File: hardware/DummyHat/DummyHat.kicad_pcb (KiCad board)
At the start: 2 copper layers, 1 part, among them U1 7404

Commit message: Finish First Dummy Hat Design
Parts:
- added D1: D, Diode_THT:D_DO-34_SOD68_P7.62mm_Horizontal, F.Cu at (58.4, 91.9)
- added D2: D, Diode_THT:D_DO-34_SOD68_P7.62mm_Horizontal, F.Cu at (81.3, 91.9)
- added D3: D, Diode_THT:D_DO-34_SOD68_P7.62mm_Horizontal, F.Cu at (81.3, 101.6)
- added D4: D, Diode_THT:D_DO-34_SOD68_P7.62mm_Horizontal, F.Cu at (58.4, 101.6)
- added D5: D, Diode_THT:D_DO-34_SOD68_P7.62mm_Horizontal, F.Cu at (66.0, 108.2)
- added D6: LED, LED_THT:LED_D5.0mm, F.Cu at (59.2, 63.5)
- added D7: LED, LED_THT:LED_D5.0mm, F.Cu at (66.3, 63.5)
- added D8: LED, LED_THT:LED_D5.0mm, F.Cu at (73.4, 63.5)
- added D9: LED, LED_THT:LED_D5.0mm, F.Cu at (80.5, 63.5)
- added J1: Conn_01x08_Socket, Connector_PinSocket_2.54mm:PinSocket_1x08_P2.54mm_Vertical, F.Cu at (61.0, 112.0)
- added J2: Conn_01x08_Socket, Connector_PinSocket_2.54mm:PinSocket_1x08_P2.54mm_Vertical, F.Cu at (61.0, 56.6)
- added J3: Conn_01x08_Socket, Connector_PinSocket_2.54mm:PinSocket_1x08_P2.54mm_Vertical, F.Cu at (61.0, 53.1)
- added R1: R, Resistor_THT:R_Axial_DIN0207_L6.3mm_D2.5mm_P10.16mm_Horizontal, F.Cu at (59.2, 66.8)
- added R2: R, Resistor_THT:R_Axial_DIN0207_L6.3mm_D2.5mm_P10.16mm_Horizontal, F.Cu at (66.3, 66.8)
- added R3: R, Resistor_THT:R_Axial_DIN0207_L6.3mm_D2.5mm_P10.16mm_Horizontal, F.Cu at (73.4, 66.8)
- added R4: R, Resistor_THT:R_Axial_DIN0207_L6.3mm_D2.5mm_P10.16mm_Horizontal, F.Cu at (80.5, 66.8)
- U1: value 7404 -> 74HC04
- moved U1 100.8 mm to (62.2, 104.6), turned to -90 degrees
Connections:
- U1 pad 1: unconnected-(U1-Pad1) -> I0
- U1 pad 11: unconnected-(U1-Pad11) -> GND
- U1 pad 12: unconnected-(U1-Pad12) -> RESP
- U1 pad 13: unconnected-(U1-Pad13) -> Net-(D1-K)
- U1 pad 2: unconnected-(U1-Pad2) -> Net-(D1-A)
- U1 pad 3: unconnected-(U1-Pad3) -> GND
- U1 pad 5: unconnected-(U1-Pad5) -> GND
- U1 pad 9: unconnected-(U1-Pad9) -> GND
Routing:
- net GND: track 0.00 -> 81.6 mm
- net Net-(D1-K): track 0.00 -> 50.6 mm
- net I0: track 0.00 -> 23.2 mm
- net I1: track 0.00 -> 21.8 mm
- net Net-(D1-A): track 0.00 -> 17.6 mm
- net I2: track 0.00 -> 13.9 mm
- net I3: track 0.00 -> 13.9 mm
- net D3: track 0.00 -> 13.7 mm
- net D2: track 0.00 -> 9.16 mm
- net RESP: track 0.00 -> 8.94 mm
- net +5V: track 0.00 -> 7.89 mm
- net D1: track 0.00 -> 5.50 mm
- net D0: track 0.00 -> 5.08 mm
- net I4: track 0.00 -> 3.81 mm
- net Net-(D9-K): track 0.00 -> 3.30 mm
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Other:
- board outline added: 38.1 x 63.5 mm

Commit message: Finish dev board. Limitations still apply.
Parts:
- added D10: LED, LED_THT:LED_D5.0mm, F.Cu at (59.4, 119.1)
- added D11: LED, LED_THT:LED_D5.0mm, F.Cu at (69.1, 119.1)
- added D12: LED, LED_THT:LED_D5.0mm, F.Cu at (78.7, 119.1)
- added D13: LED, LED_THT:LED_D5.0mm, F.Cu at (59.4, 130.3)
- added D14: LED, LED_THT:LED_D5.0mm, F.Cu at (69.1, 130.3)
- added D15: LED, LED_THT:LED_D5.0mm, F.Cu at (78.7, 130.3)
- added R10: R, Resistor_THT:R_Axial_DIN0207_L6.3mm_D2.5mm_P10.16mm_Horizontal, F.Cu at (64.3, 129.5)
- added R11: R, Resistor_THT:R_Axial_DIN0207_L6.3mm_D2.5mm_P10.16mm_Horizontal, F.Cu at (73.9, 129.5)
- added R12: R, Resistor_THT:R_Axial_DIN0207_L6.3mm_D2.5mm_P10.16mm_Horizontal, F.Cu at (83.6, 129.5)
- added R13: R, Resistor_THT:R_Axial_DIN0207_L6.3mm_D2.5mm_P10.16mm_Horizontal, F.Cu at (54.9, 133.9)
- added R14: R, Resistor_THT:R_Axial_DIN0207_L6.3mm_D2.5mm_P10.16mm_Horizontal, F.Cu at (64.0, 136.9)
- added R15: R, Resistor_THT:R_Axial_DIN0207_L6.3mm_D2.5mm_P10.16mm_Horizontal, F.Cu at (83.3, 133.9)
- added R5: R, Resistor_THT:R_Axial_DIN0207_L6.3mm_D2.5mm_P10.16mm_Horizontal, F.Cu at (83.6, 82.0)
- added R6: R, Resistor_THT:R_Axial_DIN0207_L6.3mm_D2.5mm_P10.16mm_Horizontal, F.Cu at (73.9, 82.0)
- added R7: R, Resistor_THT:R_Axial_DIN0207_L6.3mm_D2.5mm_P10.16mm_Horizontal, F.Cu at (64.3, 82.0)
- added R8: R, Resistor_THT:R_Axial_DIN0207_L6.3mm_D2.5mm_P10.16mm_Horizontal, F.Cu at (73.9, 117.1)
- added R9: R, Resistor_THT:R_Axial_DIN0207_L6.3mm_D2.5mm_P10.16mm_Horizontal, F.Cu at (83.6, 117.1)
- added U2: 74HC245, Package_DIP:DIP-20_W7.62mm, F.Cu at (56.6, 54.9)
- added U3: 74HC245, Package_DIP:DIP-20_W7.62mm, F.Cu at (83.1, 77.7)
- D1, D2, D3, D4, D5: value D -> LED; footprint Diode_THT:D_DO-34_SOD68_P7.62mm_Horizontal -> LED_THT:LED_D5.0mm
- U1: value 74HC04 -> 74HC688; footprint 7404:N14 -> Package_DIP:DIP-20_W7.62mm
- moved R1 50.5 mm to (64.3, 117.1), turned to 90 degrees
- moved D6 44.5 mm to (59.4, 108.0)
- moved U1 42.8 mm to (58.4, 147.3), turned to 90 degrees
- moved R2 41.6 mm to (83.6, 104.6), turned to 90 degrees
- moved R4 41.2 mm to (64.3, 104.7), turned to 90 degrees
- moved D9 39.4 mm to (59.4, 96.8)
- moved J1 38.6 mm to (61.0, 150.6)
- moved R3 37.8 mm to (73.9, 104.6), turned to 90 degrees
- moved D7 35.5 mm to (78.7, 96.8)
- moved D8 33.6 mm to (69.1, 96.8)
- moved J3 33.5 mm to (86.1, 75.2), turned to 180 degrees
- moved D3 27.1 mm to (59.4, 85.6), turned to 90 degrees
- moved D1 21.3 mm to (78.7, 85.6), turned to 90 degrees
- moved D2 13.7 mm to (69.1, 85.6), turned to 90 degrees
- moved D5 12.7 mm to (78.7, 108.0), turned to 90 degrees
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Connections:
- D1 pad 2: Net-(D1-A) -> D4
- D2 pad 1: Net-(D1-K) -> Net-(D2-K)
- D2 pad 2: I1 -> D5
- D3 pad 1: Net-(D1-K) -> Net-(D3-K)
- D3 pad 2: I2 -> D6
- D4 pad 1: Net-(D1-K) -> Net-(D4-K)
- D4 pad 2: I3 -> D7
- D5 pad 1: Net-(D1-K) -> Net-(D5-K)
- D5 pad 2: I4 -> D8
- J1 pad 7: RESP -> I5
- J2 pad 1: D0 -> Net-(J2-Pin_1)
- J2 pad 2: D1 -> Net-(J2-Pin_2)
- J2 pad 3: D2 -> Net-(J2-Pin_3)
- J2 pad 4: D3 -> Net-(J2-Pin_4)
- J2 pad 5: D4 -> Net-(J2-Pin_5)
- J2 pad 6: D5 -> Net-(J2-Pin_6)
- J2 pad 7: D6 -> Net-(J2-Pin_7)
- J2 pad 8: D7 -> Net-(J2-Pin_8)
- J3 pad 1: D8 -> Net-(J3-Pin_1)
- J3 pad 2: D9 -> Net-(J3-Pin_2)
- J3 pad 3: D10 -> Net-(J3-Pin_3)
- J3 pad 4: D11 -> Net-(J3-Pin_4)
- J3 pad 5: D12 -> Net-(J3-Pin_5)
- J3 pad 6: D13 -> Net-(J3-Pin_6)
- J3 pad 7: D14 -> Net-(J3-Pin_7)
- J3 pad 8: D15 -> Net-(J3-Pin_8)
- U1 pad 1: I0 -> GND
- U1 pad 10: unconnected-(U1-Pad10) -> GND
- U1 pad 11: GND -> I4
- U1 pad 12: RESP -> GND
- U1 pad 13: Net-(D1-K) -> I5
- U1 pad 14: +5V -> GND
- U1 pad 2: Net-(D1-A) -> I0
- U1 pad 3: GND -> +5V
- U1 pad 4: unconnected-(U1-Pad4) -> I1
- U1 pad 6: unconnected-(U1-Pad6) -> I2
- U1 pad 8: unconnected-(U1-Pad8) -> I3
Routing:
- net GND: track 81.6 -> 323.3 mm
- net +5V: track 7.89 -> 161.3 mm
- net Net-(U1-P=R): track 0.00 -> 131.1 mm
- net D14: track 0.00 -> 107.4 mm
- net D13: track 0.00 -> 90.8 mm
- net D12: track 0.00 -> 75.8 mm
- net D10: track 0.00 -> 71.2 mm
- net D11: track 0.00 -> 60.4 mm
- net D9: track 0.00 -> 55.7 mm
- net D1: track 5.50 -> 57.9 mm
- net D8: track 0.00 -> 50.6 mm
- net Net-(D1-K): track 50.6 -> 6.30 mm
- net D0: track 5.08 -> 46.3 mm
- net D7: track 0.00 -> 35.4 mm
- net D2: track 9.16 -> 40.1 mm
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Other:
- board size 38.1 x 63.5 mm -> 38.1 x 101.6 mm

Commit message: add not gate to dummy board for 16 data pins
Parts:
- added Q1: PN2222A, Package_TO_SOT_THT:TO-92_Inline, F.Cu at (54.7, 139.4)
- added R1: 1k, Resistor_THT:R_Axial_DIN0207_L6.3mm_D2.5mm_P10.16mm_Horizontal, F.Cu at (54.6, 131.1)
- added R2: 1k, Resistor_THT:R_Axial_DIN0207_L6.3mm_D2.5mm_P10.16mm_Horizontal, F.Cu at (54.6, 118.6)
- renumbered R1 to R16, R2 to R17
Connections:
- D1 pad 2: D4 -> D5
- D10 pad 2: D9 -> D10
- D11 pad 2: D10 -> D11
- D12 pad 2: D11 -> D12
- D13 pad 2: D12 -> D13
- D14 pad 2: D13 -> D14
- D15 pad 2: D14 -> D15
- D2 pad 2: D5 -> D6
- D3 pad 2: D6 -> D7
- D4 pad 2: D7 -> D8
- D5 pad 2: D8 -> D9
- D6 pad 2: D0 -> D1
- D7 pad 2: D1 -> D2
- D8 pad 2: D2 -> D3
- D9 pad 2: D3 -> D4
- J1 pad 7: I5 -> RESP
- U1 pad 13: I5 -> GND
- U2 pad 11: D6 -> D7
- U2 pad 12: D5 -> D6
- U2 pad 13: D4 -> D5
- U2 pad 14: D3 -> D4
- U2 pad 15: D2 -> D3
- U2 pad 16: D1 -> D2
- U2 pad 17: D0 -> D1
- U2 pad 18: Net-(J2-Pin_1) -> D0
- U2 pad 2: +5V -> Net-(J2-Pin_1)
- U3 pad 11: D14 -> D15
- U3 pad 12: D13 -> D14
- U3 pad 13: D12 -> D13
- U3 pad 14: D11 -> D12
- U3 pad 15: D10 -> D11
- U3 pad 16: D9 -> D10
- U3 pad 17: D8 -> D9
- U3 pad 18: D7 -> D8
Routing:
- net D15: track 0.00 -> 107.4 mm
- net RESP: track 0.00 -> 52.4 mm
- net D0: track 46.3 -> 0.00 mm
- net Net-(Q1-B): track 0.00 -> 31.2 mm
- net D7: track 35.4 -> 7.33 mm
- net Net-(U1-P=R): track 131.1 -> 156.2 mm
- net D2: track 40.1 -> 57.9 mm
- net D14: track 107.4 -> 90.8 mm
- net D10: track 71.2 -> 55.7 mm
- net D12: track 75.8 -> 60.4 mm
- net D8: track 50.6 -> 35.4 mm
- net D13: track 90.8 -> 75.8 mm
- net I5: track 11.8 -> 0.00 mm
- net D3: track 28.4 -> 40.1 mm
- net D1: track 57.9 -> 46.3 mm
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
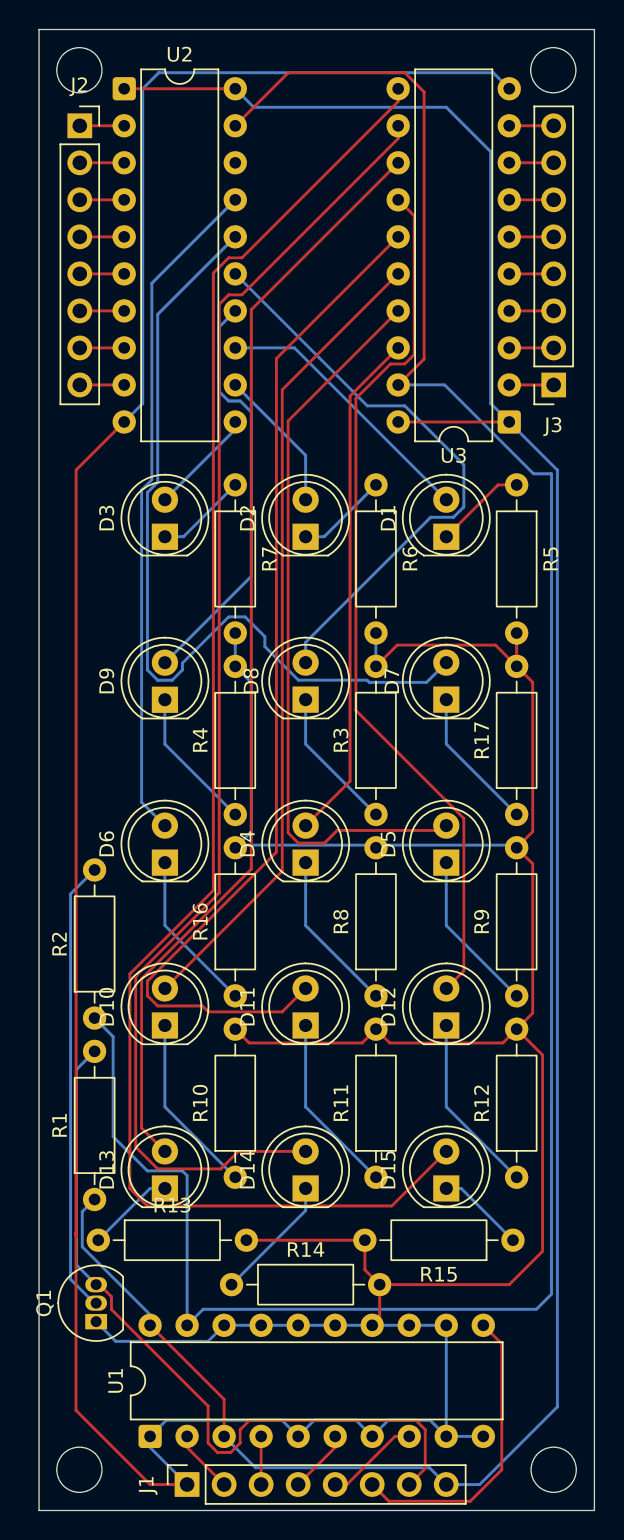
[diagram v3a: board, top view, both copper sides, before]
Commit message: cleaned up silkslides
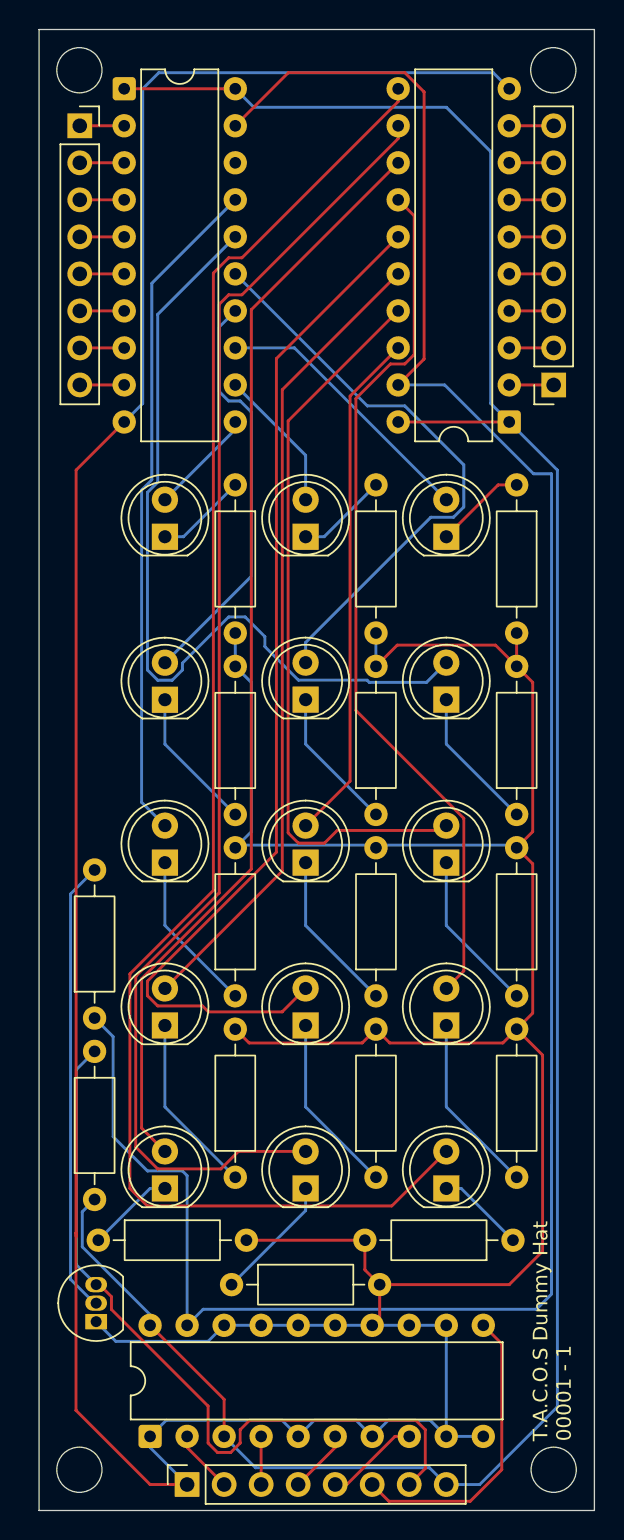
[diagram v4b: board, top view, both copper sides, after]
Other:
- board text added: "T.A.C.O.S Dummy Hat 00001 - 1"
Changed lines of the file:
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@@
 			(at 5.08 -2.37 90)
 			(layer "F.SilkS")
+			(hide yes)
 			(effects
 				(font
@@
 			(at 1.27 -3.706 90)
 			(layer "F.SilkS")
+			(hide yes)
 			(effects
 				(font
@@
 			(at 1.27 -3.56 90)
 			(layer "F.SilkS")
+			(hide yes)
 			(effects
 				(font
@@
 			(at 1.27 -3.96 90)
 			(layer "F.SilkS")
+			(hide yes)
 			(effects
 				(font
@@
 			(at 5.08 -2.37 90)
 			(layer "F.SilkS")
+			(hide yes)
 			(effects
 				(font
@@
 			(at 5.08 -2.37 90)
 			(layer "F.SilkS")
+			(hide yes)
 			(effects
 				(font
@@
 			(at 0 -2.77 0)
 			(layer "F.SilkS")
+			(hide yes)
 			(effects
 				(font
@@
 			(at 5.08 -2.37 90)
 			(layer "F.SilkS")
+			(hide yes)
 			(effects
 				(font
@@
 			(at 1.27 -3.96 90)
 			(layer "F.SilkS")
+			(hide yes)
 			(effects
 				(font
@@
 			(at 5.08 -2.37 0)
 			(layer "F.SilkS")
+			(hide yes)
 			(effects
 				(font
@@
 			(at 5.08 -2.37 90)
 			(layer "F.SilkS")
+			(hide yes)
 			(effects
 				(font
@@
 			(at 1.27 -3.96 90)
 			(layer "F.SilkS")
+			(hide yes)
 			(effects
 				(font
@@
 			(at 3.81 -2.33 0)
 			(layer "F.SilkS")
+			(hide yes)
 			(effects
 				(font
@@
 			(at 5.08 -2.37 0)
 			(layer "F.SilkS")
+			(hide yes)
 			(effects
 				(font
@@
 			(at 5.08 -2.37 90)
 			(layer "F.SilkS")
+			(hide yes)
 			(effects
 				(font
@@
 			(at 5.08 -2.37 90)
 			(layer "F.SilkS")
+			(hide yes)
 			(effects
 				(font
@@
 			(at 1.27 -3.706 90)
 			(layer "F.SilkS")
+			(hide yes)
 			(effects
 				(font
@@
 			(at 5.08 -2.37 90)
 			(layer "F.SilkS")
+			(hide yes)
 			(effects
 				(font
@@
 			(at 5.08 -2.37 90)
 			(layer "F.SilkS")
+			(hide yes)
 			(effects
 				(font
@@
 			(at 5.08 -2.37 90)
 			(layer "F.SilkS")
+			(hide yes)
 			(effects
 				(font
@@
 			(at 1.27 -3.96 90)
 			(layer "F.SilkS")
+			(hide yes)
 			(effects
 				(font
@@
 			(at 5.08 -2.37 90)
 			(layer "F.SilkS")
+			(hide yes)
 			(effects
 				(font
@@
 			(at 1.27 -3.96 90)
 			(layer "F.SilkS")
+			(hide yes)
 			(effects
 				(font
@@
 			(at 1.27 -3.96 90)
 			(layer "F.SilkS")
+			(hide yes)
 			(effects
 				(font
@@
 			(at 5.08 -2.37 90)
 			(layer "F.SilkS")
+			(hide yes)
 			(effects
 				(font
@@
 			(at 1.27 -3.96 90)
 			(layer "F.SilkS")
+			(hide yes)
 			(effects
 				(font
@@
 			(at 1.27 -3.96 90)
 			(layer "F.SilkS")
+			(hide yes)
 			(effects
 				(font
@@
 			(at 1.27 -3.96 90)
 			(layer "F.SilkS")
+			(hide yes)
 			(effects
 				(font
@@
 			(at 1.27 -3.96 90)
 			(layer "F.SilkS")
+			(hide yes)
 			(effects
 				(font
@@
 			(at 0 -2.77 0)
 			(layer "F.SilkS")
+			(hide yes)
 			(effects
 				(font
@@
 			(at 1.27 -3.96 90)
 			(layer "F.SilkS")
+			(hide yes)
 			(effects
 				(font
@@
 			(at 1.27 -3.96 90)
 			(layer "F.SilkS")
+			(hide yes)
 			(effects
 				(font
@@
 			(at 5.08 -2.37 0)
 			(layer "F.SilkS")
+			(hide yes)
 			(effects
 				(font
@@
 			(at 0 -2.77 90)
 			(layer "F.SilkS")
+			(hide yes)
 			(effects
 				(font
@@
 			(at 5.08 -2.37 90)
 			(layer "F.SilkS")
+			(hide yes)
 			(effects
 				(font
@@
 			(at 1.27 -3.96 90)
 			(layer "F.SilkS")
+			(hide yes)
 			(effects
 				(font
@@
 			(at 3.81 -2.33 0)
 			(layer "F.SilkS")
+			(hide yes)
 			(effects
 				(font
@@
 			(at 5.08 -2.37 90)
 			(layer "F.SilkS")
+			(hide yes)
 			(effects
 				(font
@@
 			(at 3.81 -2.33 90)
 			(layer "F.SilkS")
+			(hide yes)
 			(effects
 				(font
@@
 		(layer "Edge.Cuts")
 	)
+	(gr_text "T.A.C.O.S Dummy Hat\n00001 - 1"
+		(at 87.4014 147.6502 90)
+		(layer "F.SilkS")
+		(effects
+			(font
+				(size 1 1)
+				(thickness 0.1)
+			)
+			(justify left bottom)
+		)
+	)
 	(dimension
